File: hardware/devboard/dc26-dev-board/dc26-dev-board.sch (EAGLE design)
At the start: 41 parts, among them IC1 STM32F411RET6, IC10 APA104, IC11 APA104, IC12 APA104, IC13 APA104, IC14 APA104, IC15 APA104, IC16 APA104, IC2 APA104, IC3 APA104, IC4 APA104, IC5 APA104, IC6 APA104, IC7 APA104, IC8 APA104, IC9 APA104, U1 ESP-WROOM-32, Y1 ABL-8.000MHZ-B2

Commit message: all but breakouts are done (I think)
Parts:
- added C13: 10uF, dc-26:C-USC0805
- added ENABLE: SW2, dc-26:SWITCH_TACTILETACTILE-2PIN-NARROW
- added ESP-BREAKOUT, STM32-BREAKOUT: M20X2, dc-26:M20X2
- added ESP32-PROGRAM-HEADER: SERIAL_4, dc-26:SERIAL_4
- added R1, R4: 10K, dc-26:RESISTOR1206
- added RESET: SW1, dc-26:SWITCH_TACTILETACTILE-2PIN-NARROW
- added Z1: CMDZ3L3_TR, dc-26:CMDZ3L3_TR
- U1: device esp32:ESP-WROOM-32 -> dc-26:ESP-WROOM-32
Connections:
- new net ESP-EN: ENABLE.A, R4.1, U1.EN
- new net ESP-IO0: R1.1, RESET.A, U1.IO0
- new net ESP-RX: ESP32-PROGRAM-HEADER.RX, Z1.K
- new net ESP-RX0: U1.RXD0, Z1.A
- new net ESP-TX0: U1.TXD0
- new net ESP-TXD0: ESP32-PROGRAM-HEADER.TX
- net GND: now also C13.2, ENABLE.C, ESP32-PROGRAM-HEADER.GND, RESET.C, U1.GND, U1.GND@1, U1.GND@15, U1.GND@38, U1.IO2
- net VCC: now also ESP32-PROGRAM-HEADER.VCC, R1.2, R4.2, U1.3V3
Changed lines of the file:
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@@
 </classes>
 <parts>
-<part name="U1" library="esp32" deviceset="ESP-WROOM-32" device=""/>
 <part name="Y1" library="ABL-8.000MHZ-B2" deviceset="ABL-8.000MHZ-B2" device=""/>
 <part name="IC1" library="STM32F411RET6" deviceset="STM32F411RET6" device=""/>
@@
 <part name="SUPPLY12" library="dc-26" deviceset="VCC" device="" value="VDDA"/>
 <part name="VSSA" library="dc-26" deviceset="GND" device="" value="VSSA"/>
+<part name="U1" library="dc-26" deviceset="ESP-WROOM-32" device=""/>
+<part name="GND11" library="dc-26" deviceset="GND" device=""/>
+<part name="C13" library="dc-26" deviceset="C-US" device="C0805" value="10uF"/>
+<part name="GND13" library="dc-26" deviceset="GND" device=""/>
+<part name="SUPPLY13" library="dc-26" deviceset="VCC" device=""/>
+<part name="ESP32-PROGRAM-HEADER" library="dc-26" deviceset="SERIAL_4" device=""/>
+<part name="Z1" library="dc-26" deviceset="CMDZ3L3_TR" device=""/>
+<part name="GND14" library="dc-26" deviceset="GND" device=""/>
+<part name="GND15" library="dc-26" deviceset="GND" device=""/>
+<part name="GND16" library="dc-26" deviceset="GND" device=""/>
+<part name="GND17" library="dc-26" deviceset="GND" device=""/>
+<part name="ENABLE" library="dc-26" deviceset="SWITCH_TACTILE" device="TACTILE-2PIN-NARROW" value="SW2"/>
+<part name="RESET" library="dc-26" deviceset="SWITCH_TACTILE" device="TACTILE-2PIN-NARROW" value="SW1"/>
+<part name="GND18" library="dc-26" deviceset="GND" device=""/>
+<part name="GND19" library="dc-26" deviceset="GND" device=""/>
+<part name="R1" library="dc-26" deviceset="RESISTOR" device="1206" value="10K"/>
+<part name="R4" library="dc-26" deviceset="RESISTOR" device="1206" value="10K"/>
+<part name="SUPPLY14" library="dc-26" deviceset="VCC" device=""/>
+<part name="SUPPLY15" library="dc-26" deviceset="VCC" device=""/>
+<part name="ESP-BREAKOUT" library="dc-26" deviceset="M20X2" device=""/>
+<part name="STM32-BREAKOUT" library="dc-26" deviceset="M20X2" device=""/>
 </parts>
 <sheets>
@@
 </plain>
 <instances>
-<instance part="U1" gate="G$1" x="-12.7" y="45.72"/>
 <instance part="Y1" gate="G$1" x="50.8" y="71.12" rot="R90"/>
 <instance part="IC1" gate="G$1" x="73.66" y="66.04"/>
@@
 <instance part="SUPPLY12" gate="G$1" x="104.14" y="-17.78" rot="R270"/>
 <instance part="VSSA" gate="1" x="106.68" y="-27.94" rot="R90"/>
+<instance part="U1" gate="G$1" x="-5.08" y="63.5"/>
+<instance part="GND11" gate="1" x="2.54" y="38.1"/>
+<instance part="C13" gate="G$1" x="-40.64" y="53.34"/>
+<instance part="GND13" gate="1" x="-40.64" y="40.64"/>
+<instance part="SUPPLY13" gate="G$1" x="-40.64" y="68.58"/>
+<instance part="ESP32-PROGRAM-HEADER" gate="G$1" x="-17.78" y="-15.24" rot="R90"/>
+<instance part="Z1" gate="G$1" x="17.78" y="-12.7" rot="R90"/>
+<instance part="GND14" gate="1" x="-25.4" y="71.12" rot="R180"/>
+<instance part="GND15" gate="1" x="33.02" y="66.04" rot="R90"/>
+<instance part="GND16" gate="1" x="12.7" y="17.78"/>
+<instance part="GND17" gate="1" x="-10.16" y="17.78"/>
+<instance part="ENABLE" gate="G$1" x="-35.56" y="104.14"/>
+<instance part="RESET" gate="G$1" x="-60.96" y="104.14"/>
+<instance part="GND18" gate="1" x="-60.96" y="93.98"/>
+<instance part="GND19" gate="1" x="-35.56" y="93.98"/>
+<instance part="R1" gate="G$1" x="-50.8" y="127" rot="R90"/>
+<instance part="R4" gate="G$1" x="-25.4" y="124.46" rot="R90"/>
+<instance part="SUPPLY14" gate="G$1" x="-50.8" y="142.24"/>
+<instance part="SUPPLY15" gate="G$1" x="-25.4" y="142.24"/>
+<instance part="ESP-BREAKOUT" gate="G$1" x="-96.52" y="40.64"/>
+<instance part="STM32-BREAKOUT" gate="G$1" x="271.78" y="43.18"/>
 </instances>
 <busses>
@@
 <pinref part="U$1" gate="G$1" pin="GND"/>
 <wire x1="180.34" y1="60.96" x2="175.26" y2="60.96" width="0.1524" layer="91"/>
+</segment>
+<segment>
+<pinref part="U1" gate="G$1" pin="GND"/>
+<wire x1="2.54" y1="45.72" x2="2.54" y2="40.64" width="0.1524" layer="91"/>
+<pinref part="GND11" gate="1" pin="GND"/>
+</segment>
+<segment>
+<pinref part="C13" gate="G$1" pin="2"/>
+<wire x1="-40.64" y1="48.26" x2="-40.64" y2="43.18" width="0.1524" layer="91"/>
+<pinref part="GND13" gate="1" pin="GND"/>
+<wire x1="-40.64" y1="43.18" x2="-40.64" y2="40.64" width="0.1524" layer="91"/>
+<junction x="-40.64" y="43.18"/>
+</segment>
+<segment>
+<pinref part="ESP32-PROGRAM-HEADER" gate="G$1" pin="GND"/>
+<wire x1="-12.7" y1="-7.62" x2="-12.7" y2="-5.08" width="0.1524" layer="91"/>
+</segment>
+<segment>
+<pinref part="U1" gate="G$1" pin="GND@1"/>
+<wire x1="-22.86" y1="66.04" x2="-25.4" y2="66.04" width="0.1524" layer="91"/>
+<wire x1="-25.4" y1="66.04" x2="-25.4" y2="68.58" width="0.1524" layer="91"/>
+<pinref part="GND14" gate="1" pin="GND"/>
+</segment>
+<segment>
+<pinref part="U1" gate="G$1" pin="GND@38"/>
+<wire x1="25.4" y1="66.04" x2="30.48" y2="66.04" width="0.1524" layer="91"/>
+<pinref part="GND15" gate="1" pin="GND"/>
+</segment>
+<segment>
+<pinref part="U1" gate="G$1" pin="IO2"/>
+<wire x1="12.7" y1="22.86" x2="12.7" y2="20.32" width="0.1524" layer="91"/>
+<pinref part="GND16" gate="1" pin="GND"/>
+<wire x1="12.7" y1="20.32" x2="12.7" y2="17.78" width="0.1524" layer="91"/>
+<junction x="12.7" y="20.32"/>
+</segment>
+<segment>
+<pinref part="U1" gate="G$1" pin="GND@15"/>
+<wire x1="-10.16" y1="22.86" x2="-10.16" y2="20.32" width="0.1524" layer="91"/>
+<pinref part="GND17" gate="1" pin="GND"/>
+<wire x1="-10.16" y1="20.32" x2="-10.16" y2="17.78" width="0.1524" layer="91"/>
+<junction x="-10.16" y="20.32"/>
+</segment>
+<segment>
+<pinref part="ENABLE" gate="G$1" pin="C"/>
+<pinref part="GND19" gate="1" pin="GND"/>
+<wire x1="-35.56" y1="96.52" x2="-35.56" y2="99.06" width="0.1524" layer="91"/>
+</segment>
+<segment>
+<pinref part="RESET" gate="G$1" pin="C"/>
+<pinref part="GND18" gate="1" pin="GND"/>
+<wire x1="-60.96" y1="96.52" x2="-60.96" y2="99.06" width="0.1524" layer="91"/>
 </segment>
 </net>
@@
 <wire x1="180.34" y1="66.04" x2="175.26" y2="66.04" width="0.1524" layer="91"/>
 </segment>
+<segment>
+<pinref part="U1" gate="G$1" pin="3V3"/>
+<wire x1="-22.86" y1="63.5" x2="-40.64" y2="63.5" width="0.1524" layer="91"/>
+<wire x1="-40.64" y1="63.5" x2="-40.64" y2="68.58" width="0.1524" layer="91"/>
+<wire x1="-40.64" y1="63.5" x2="-40.64" y2="55.88" width="0.1524" layer="91"/>
+<pinref part="SUPPLY13" gate="G$1" pin="VCC"/>
+</segment>
+<segment>
+<pinref part="ESP32-PROGRAM-HEADER" gate="G$1" pin="VCC"/>
+<wire x1="-20.32" y1="-7.62" x2="-20.32" y2="-5.08" width="0.1524" layer="91"/>
+</segment>
+<segment>
+<pinref part="R1" gate="G$1" pin="2"/>
+<wire x1="-50.8" y1="132.08" x2="-50.8" y2="142.24" width="0.1524" layer="91"/>
+<pinref part="SUPPLY14" gate="G$1" pin="VCC"/>
+</segment>
+<segment>
+<pinref part="R4" gate="G$1" pin="2"/>
+<wire x1="-25.4" y1="129.54" x2="-25.4" y2="142.24" width="0.1524" layer="91"/>
+<pinref part="SUPPLY15" gate="G$1" pin="VCC"/>
+</segment>
 </net>
 <net name="N$6" class="0">
@@
 </segment>
 </net>
+<net name="ESP-RX" class="0">
+<segment>
+<pinref part="ESP32-PROGRAM-HEADER" gate="G$1" pin="RX"/>
+<wire x1="-17.78" y1="-7.62" x2="-17.78" y2="-5.08" width="0.1524" layer="91"/>
+<label x="-17.78" y="-5.08" size="1.778" layer="95" rot="R90"/>
+</segment>
+<segment>
+<pinref part="Z1" gate="G$1" pin="K"/>
+<wire x1="17.78" y1="-12.7" x2="17.78" y2="-17.78" width="0.1524" layer="91"/>
+<label x="20.32" y="-17.78" size="1.778" layer="95"/>
+</segment>
+</net>
+<net name="ESP-TXD0" class="0">
+<segment>
+<pinref part="ESP32-PROGRAM-HEADER" gate="G$1" pin="TX"/>
+<wire x1="-15.24" y1="-7.62" x2="-15.24" y2="-5.08" width="0.1524" layer="91"/>
+<label x="-15.24" y="-5.08" size="1.778" layer="95" rot="R90"/>
+</segment>
+</net>
+<net name="ESP-RX0" class="0">
+<segment>
+<pinref part="Z1" gate="G$1" pin="A"/>
+<wire x1="17.78" y1="2.54" x2="17.78" y2="7.62" width="0.1524" layer="91"/>
+<label x="20.32" y="7.62" size="1.778" layer="95"/>
+</segment>
+<segment>
+<pinref part="U1" gate="G$1" pin="RXD0"/>
+<wire x1="25.4" y1="55.88" x2="33.02" y2="55.88" width="0.1524" layer="91"/>
+<label x="33.02" y="55.88" size="1.778" layer="95"/>
+</segment>
+</net>
+<net name="ESP-TX0" class="0">
+<segment>
+<pinref part="U1" gate="G$1" pin="TXD0"/>
+<wire x1="25.4" y1="58.42" x2="33.02" y2="58.42" width="0.1524" layer="91"/>
+<label x="33.02" y="58.42" size="1.778" layer="95"/>
+</segment>
+</net>
+<net name="ESP-EN" class="0">
+<segment>
+<pinref part="ENABLE" gate="G$1" pin="A"/>
+<wire x1="-35.56" y1="109.22" x2="-35.56" y2="114.3" width="0.1524" layer="91"/>
+<wire x1="-35.56" y1="114.3" x2="-25.4" y2="114.3" width="0.1524" layer="91"/>
+<wire x1="-25.4" y1="114.3" x2="-25.4" y2="104.14" width="0.1524" layer="91"/>
+<pinref part="R4" gate="G$1" pin="1"/>
+<wire x1="-25.4" y1="114.3" x2="-25.4" y2="119.38" width="0.1524" layer="91"/>
+<junction x="-25.4" y="114.3"/>
+<label x="-25.4" y="96.52" size="1.778" layer="95" rot="R90"/>
+</segment>
+<segment>
+<pinref part="U1" gate="G$1" pin="EN"/>
+<wire x1="-22.86" y1="60.96" x2="-25.4" y2="60.96" width="0.1524" layer="91"/>
+<label x="-33.02" y="60.96" size="1.778" layer="95"/>
+</segment>
+</net>
+<net name="ESP-IO0" class="0">
+<segment>
+<pinref part="RESET" gate="G$1" pin="A"/>
+<wire x1="-60.96" y1="109.22" x2="-60.96" y2="116.84" width="0.1524" layer="91"/>
+<wire x1="-60.96" y1="116.84" x2="-50.8" y2="116.84" width="0.1524" layer="91"/>
+<wire x1="-50.8" y1="116.84" x2="-50.8" y2="104.14" width="0.1524" layer="91"/>
+<pinref part="R1" gate="G$1" pin="1"/>
+<wire x1="-50.8" y1="116.84" x2="-50.8" y2="121.92" width="0.1524" layer="91"/>
+<junction x="-50.8" y="116.84"/>
+<label x="-50.8" y="96.52" size="1.778" layer="95" rot="R90"/>
+</segment>
+<segment>
+<pinref part="U1" gate="G$1" pin="IO0"/>
+<wire x1="25.4" y1="33.02" x2="30.48" y2="33.02" width="0.1524" layer="91"/>
+<label x="33.02" y="33.02" size="1.778" layer="95"/>
+</segment>
+</net>

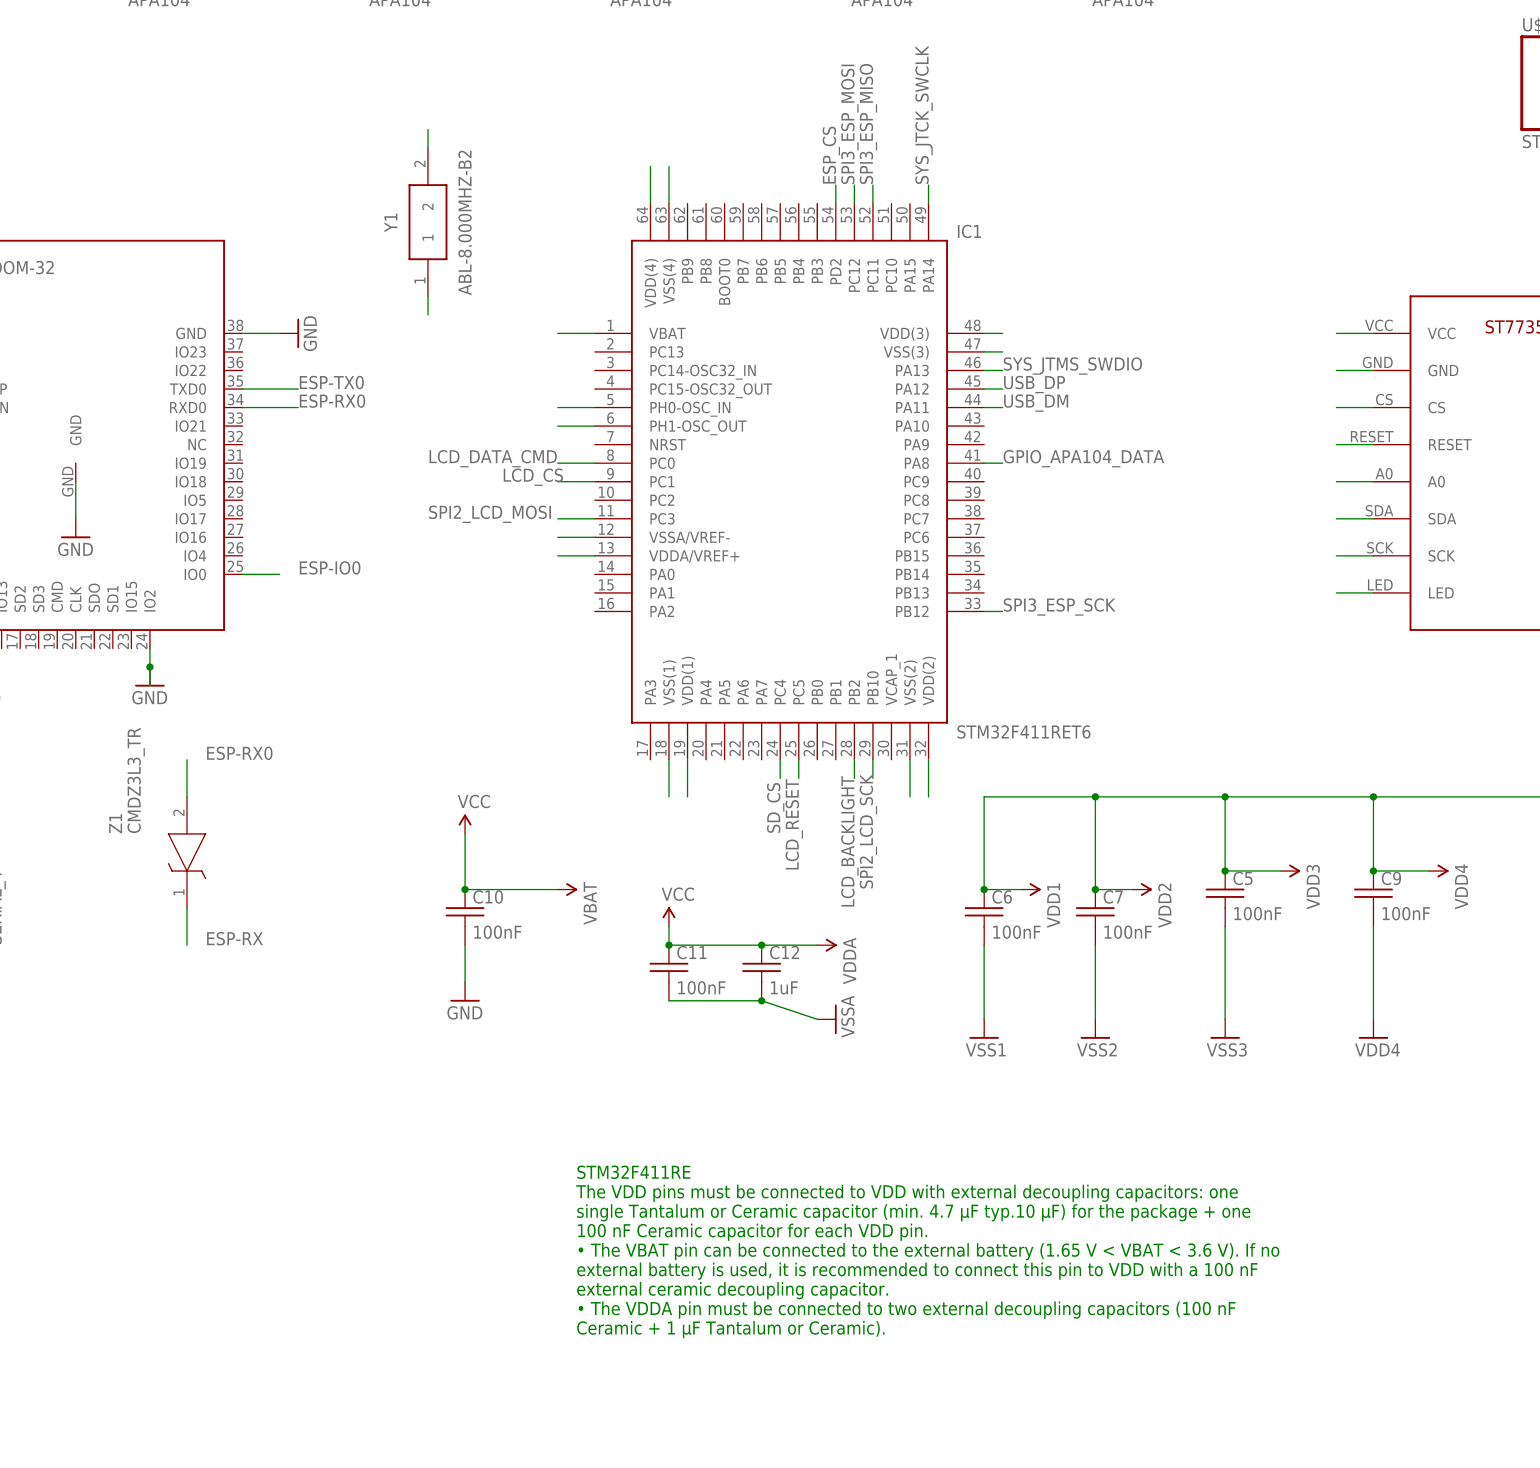
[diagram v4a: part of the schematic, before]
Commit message: added ferrite bead updated VSS to go to gnd
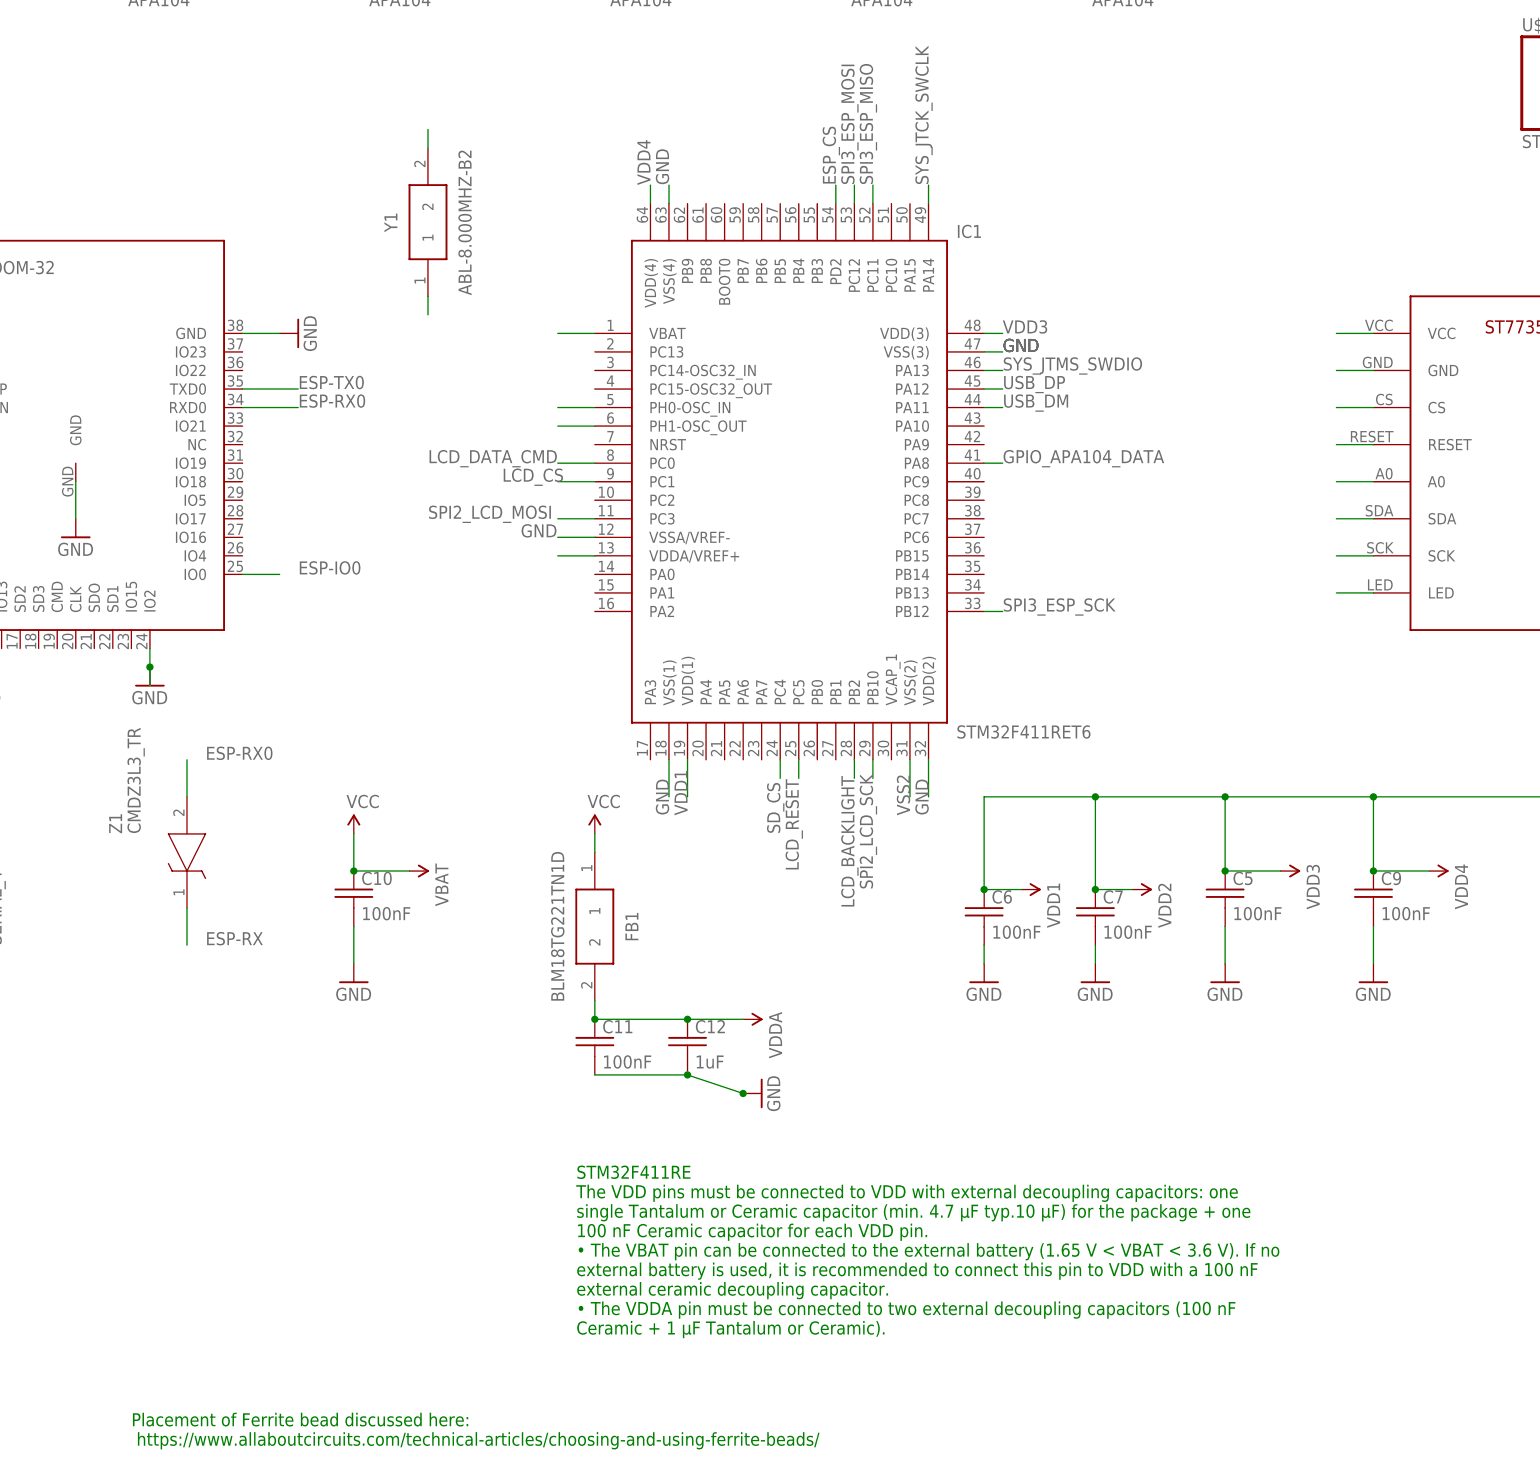
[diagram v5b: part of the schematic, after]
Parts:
- added FB1: BLM18TG221TN1D, dc-26:BLM18TG221TN1D
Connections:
- removed net VDD2: IC1.VDD(2)
- removed net VSS1: C6.2, IC1.VSS(1)
- removed net VSS3: C5.2, IC1.VSS(3)
- removed net VSS4: C9.2, IC1.VSS(4)
- removed net VSSA: C11.2, C12.2, IC1.VSSA/VREF-
- net GND: now also C11.2, C12.2, C5.2, C6.2, C7.2, C9.2, IC1.VDD(2), IC1.VSS(1), IC1.VSS(3), IC1.VSS(4), IC1.VSSA/VREF-
- net VCC: now also FB1.1, FB1.2
- net VSS2: no longer C7.2
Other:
- note added: "Placement of Ferrite bead discussed here: https://www.allaboutcircuits.com/technical-articles/choosing-and-using-ferrite-beads/"
- moved on the sheet: C10, C11, C12

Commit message: changed caps to 8050 rather than 1205 per https://www.allaboutcircuits.com/technical-articles/clean-power-for-every-ic-part-2-choosing-and-using-your-bypass-capacitors/
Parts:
- C1, C2: device dc-26:C-USC1210 -> dc-26:C-USC0805
- C10, C11, C12, C3, C4, C5, C6, C7, C8, C9: device dc-26:C-USC1206 -> dc-26:C-USC0805
